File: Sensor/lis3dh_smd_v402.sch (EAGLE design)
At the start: 7 parts, among them U5 LIS3DHTR

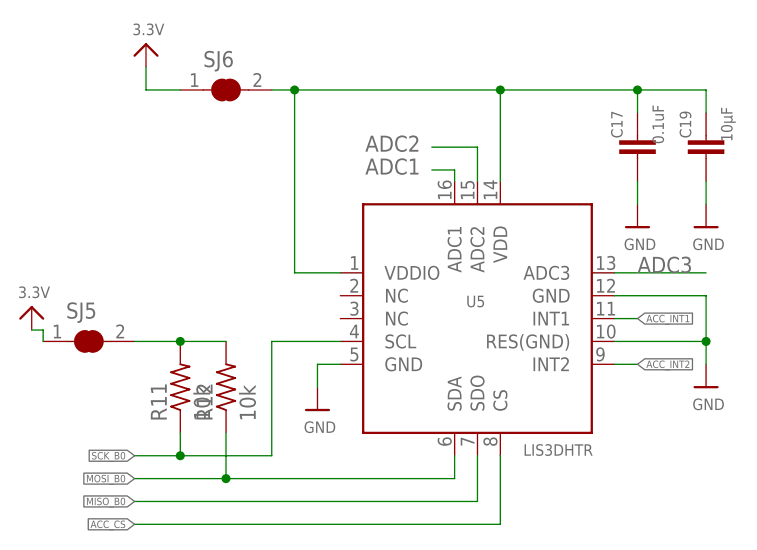
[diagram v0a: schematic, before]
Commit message: accelerometer updated
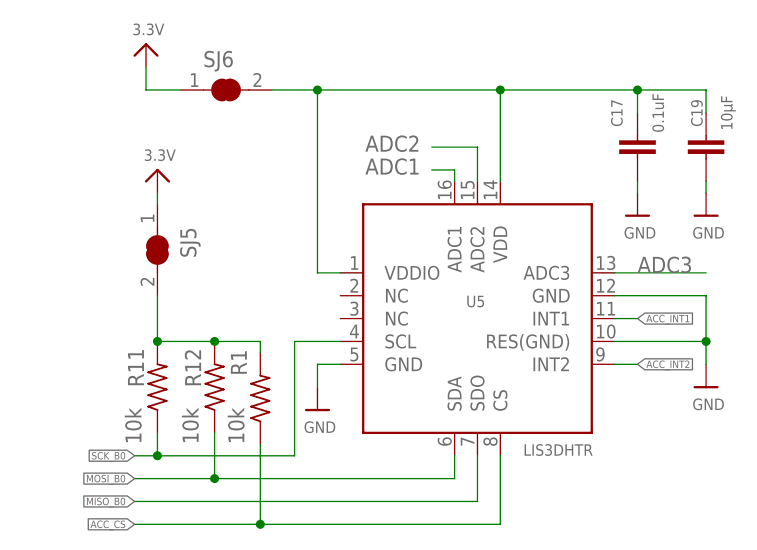
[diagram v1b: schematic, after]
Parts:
- added R1: 10k, rcl-2:R-US_R0402
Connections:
- net ACC_CS: now also R1.1
- net N$2: now also R1.2
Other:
- moved on the sheet: R11, R12, SJ5
